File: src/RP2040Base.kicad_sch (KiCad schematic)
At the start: 14 parts, among them J1 USB4500-03-0-A, U1 RT6154AGQW

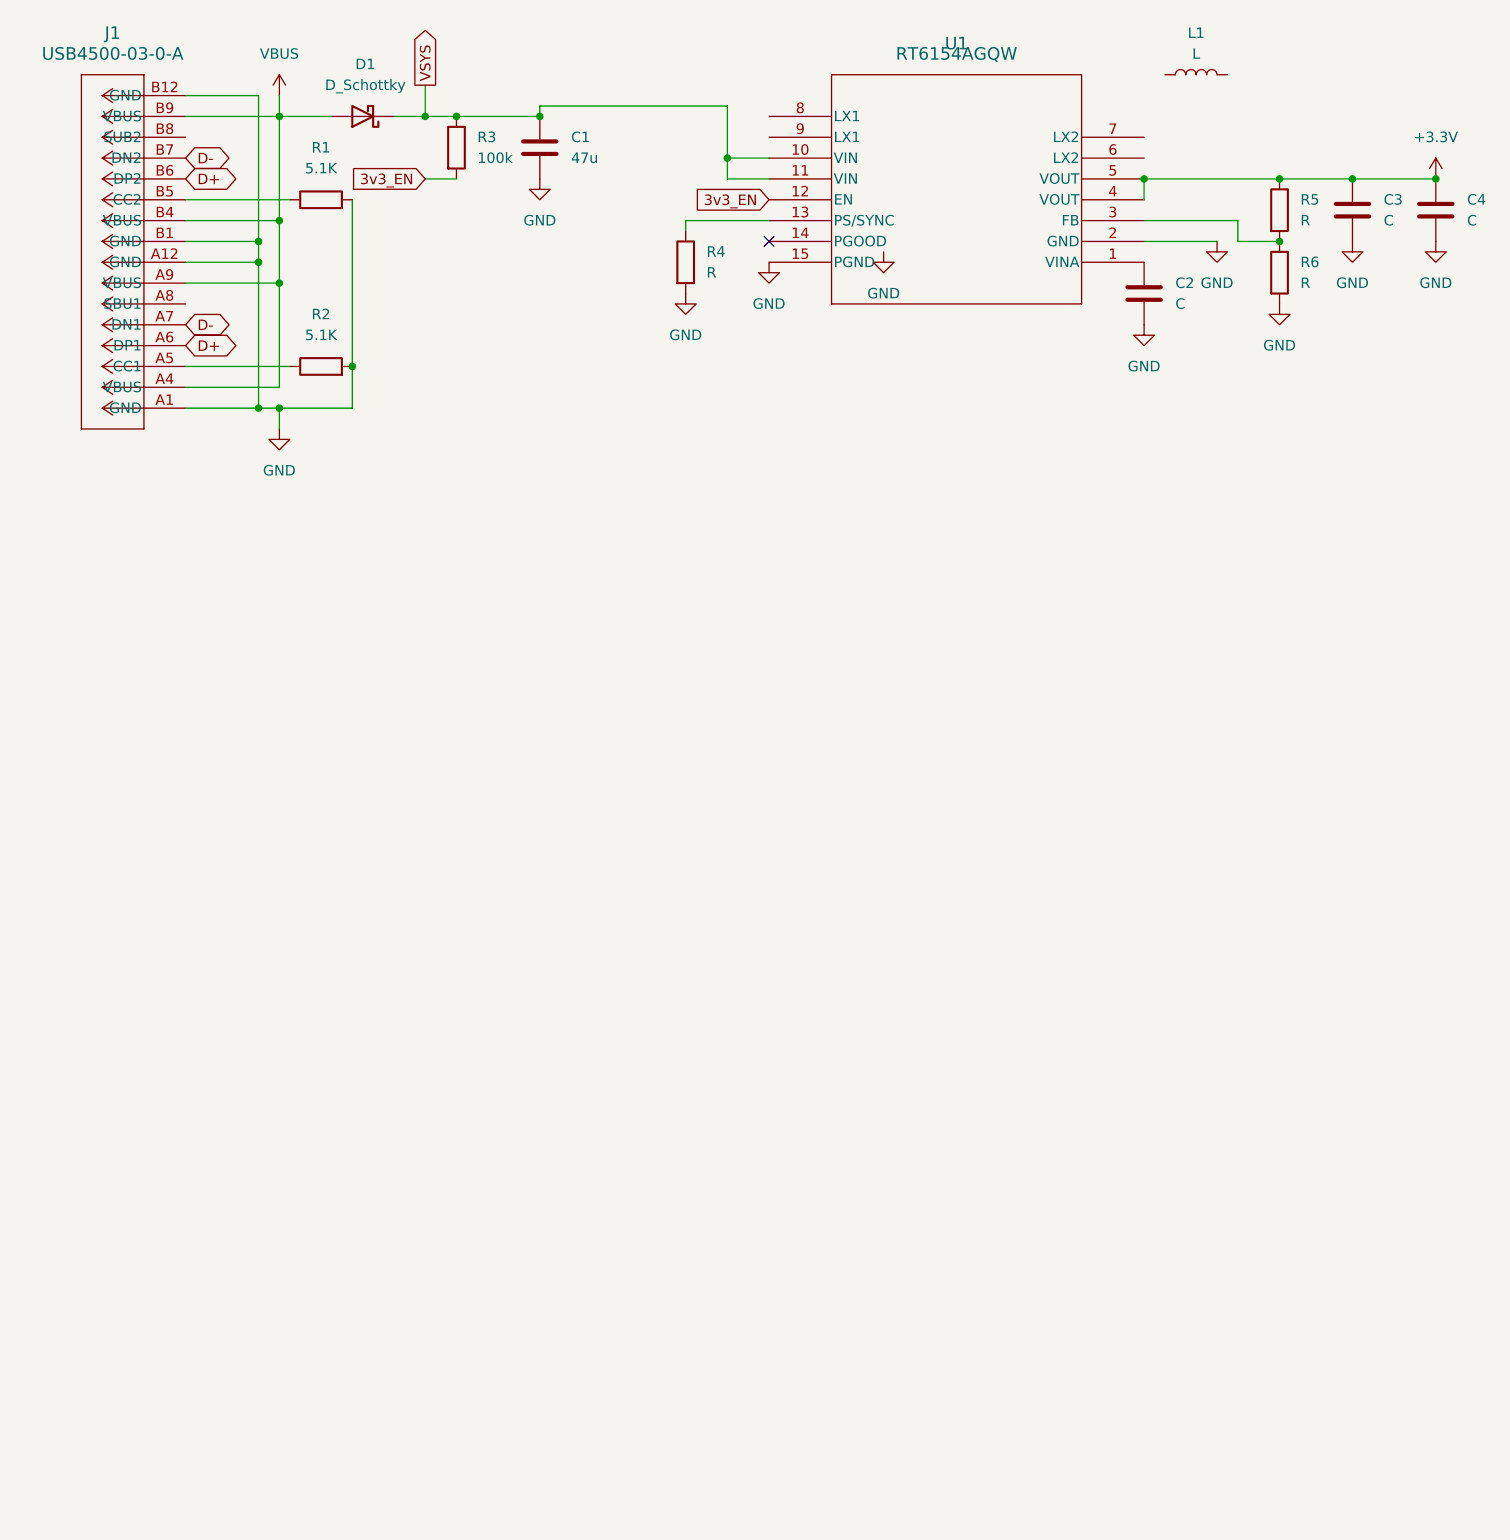
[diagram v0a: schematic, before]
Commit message: Adding Oscillator, flash, and MCU
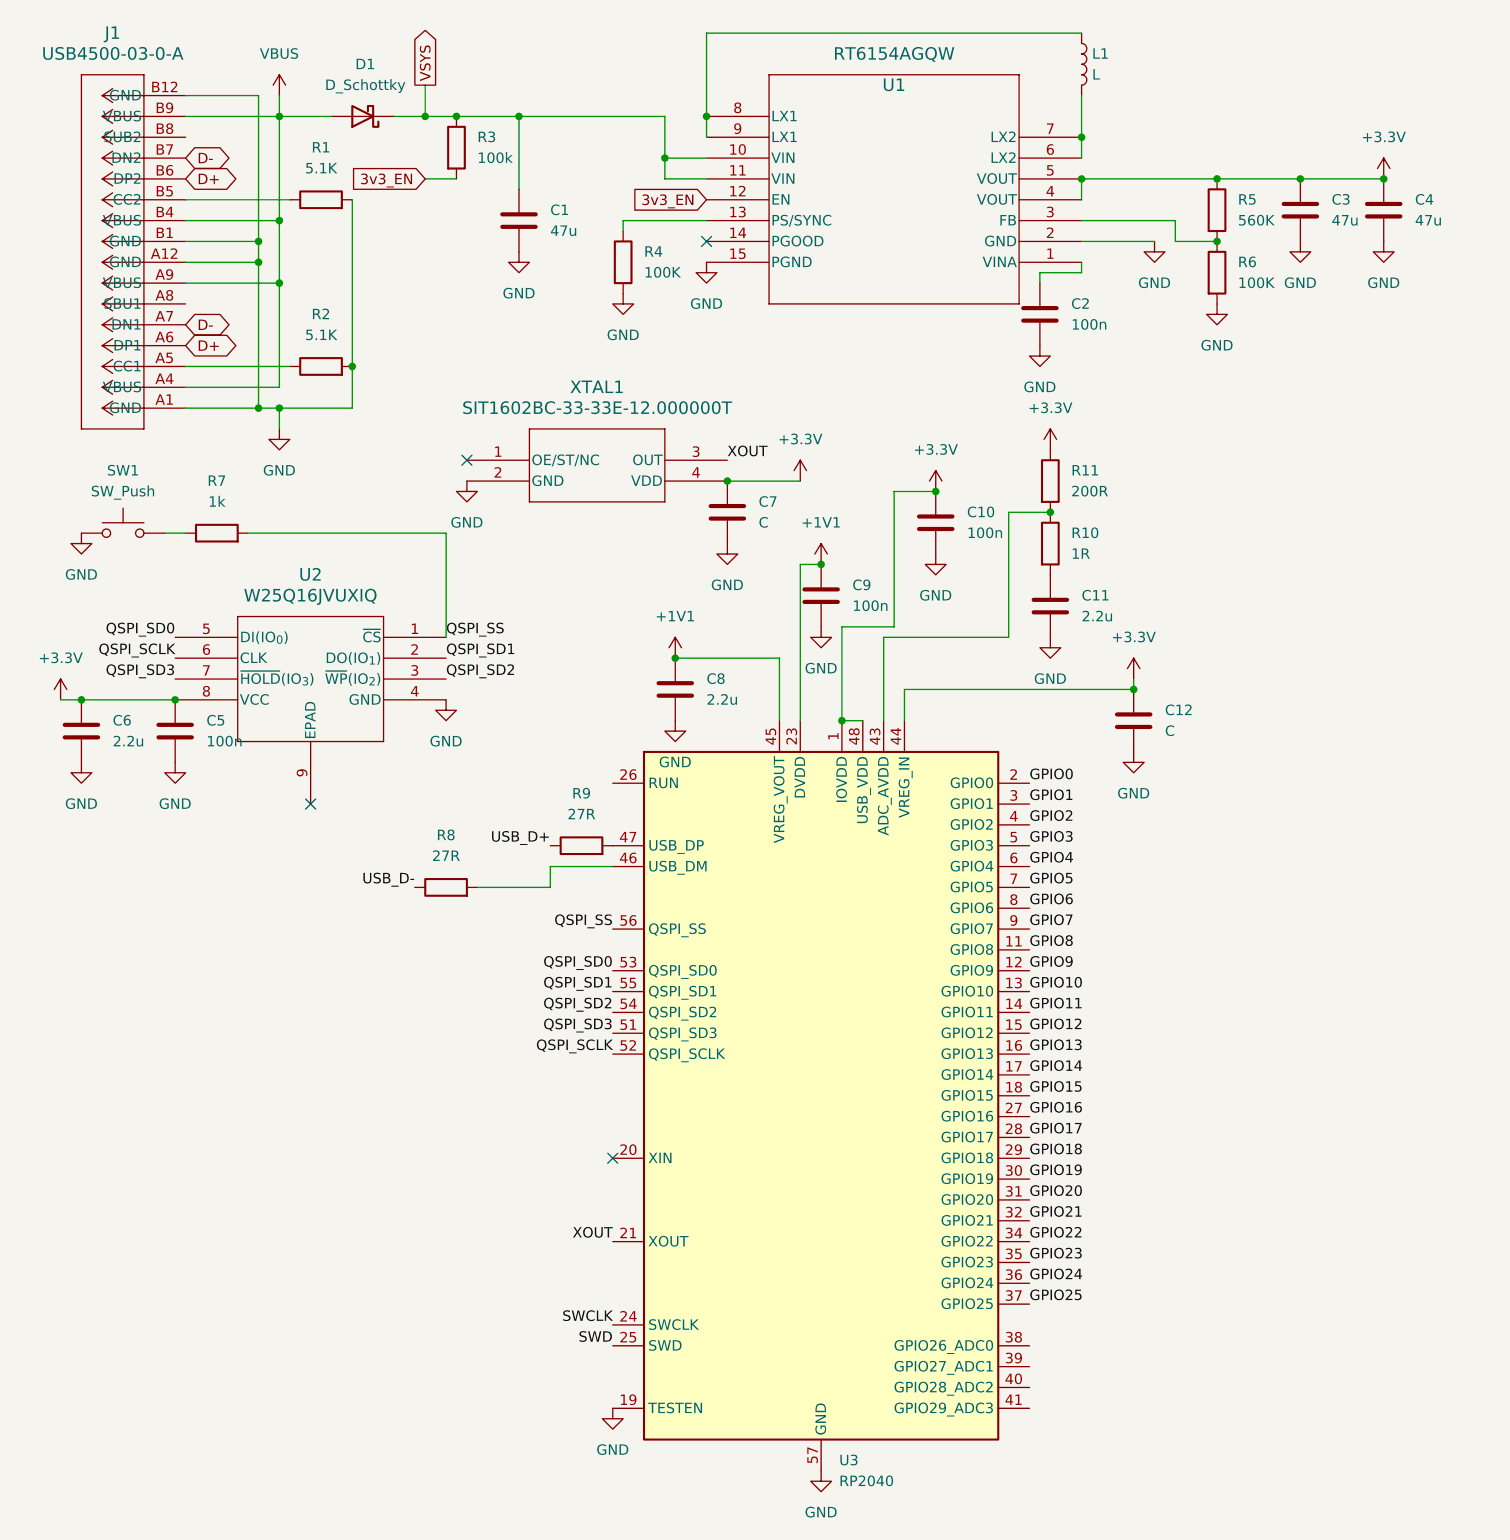
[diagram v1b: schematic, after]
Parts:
- added C10, C5, C9: 100n, symbol Device:C
- added C11, C6, C8: 2.2u, symbol Device:C
- added C12, C7: C, symbol Device:C
- added R10: 1R, symbol Device:R
- added R11: 200R, symbol Device:R
- added R7: 1k, symbol Device:R
- added R8, R9: 27R, symbol Device:R
- added SW1: SW_Push, symbol Switch:SW_Push
- added U2: W25Q16JVUXIQ, W25Q16JVUXIQ_WIN, symbol W25Q16JVUXIQ:W25Q16JVUXIQ
- added U3: RP2040, Package_DFN_QFN:QFN-56-1EP_7x7mm_P0.4mm_EP3.2x3.2mm, symbol MCU_RaspberryPi:RP2040
- added XTAL1: SIT1602BC-33-33E-12.000000T, SON4_SIT1602-3_SIT, symbol SIT1602BC:SIT1602BC-33-33E-12.000000T
- C2: value C -> 100n
- C3, C4: value C -> 47u
- R4, R6: value R -> 100K
- R5: value R -> 560K
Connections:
- net +3.3V: now also C10.1, C12.1, C5.1, C6.1, C7.1, R11.1, U2.8 (VCC), U3.1 (IOVDD), U3.10 (IOVDD), U3.22 (IOVDD), U3.33 (IOVDD), U3.42 (IOVDD), U3.44 (VREG_IN), U3.48 (USB_VDD), U3.49 (IOVDD), XTAL1.4 (VDD)
- net GND: now also C10.2, C11.2, C12.2, C5.2, C6.2, C7.2, C8.2, C9.2, SW1.1, U2.4 (GND), U3.19 (TESTEN), U3.57 (GND), XTAL1.2 (GND)
- net at U1.6 (LX2): now also L1.2, U1.7 (LX2)
- net at U1.8 (LX1): now also L1.1, U1.9 (LX1)
- new net: R10.1, R11.2, U3.43 (ADC_AVDD)
- new net: C11.1, R10.2
- new net: R9.2, U3.47 (USB_DP)
- new net: R8.2, U3.46 (USB_DM)
- new net: R7.1, SW1.2
- new net +1V1: C8.1, C9.1, U3.23 (DVDD), U3.45 (VREG_VOUT), U3.50 (DVDD)
- new net GPIO0: U3.2 (GPIO0)
- new net GPIO1: U3.3 (GPIO1)
- new net GPIO10: U3.13 (GPIO10)
- new net GPIO11: U3.14 (GPIO11)
- new net GPIO12: U3.15 (GPIO12)
- new net GPIO13: U3.16 (GPIO13)
- new net GPIO14: U3.17 (GPIO14)
- new net GPIO15: U3.18 (GPIO15)
- new net GPIO16: U3.27 (GPIO16)
- new net GPIO17: U3.28 (GPIO17)
- new net GPIO18: U3.29 (GPIO18)
- new net GPIO19: U3.30 (GPIO19)
- new net GPIO2: U3.4 (GPIO2)
- new net GPIO20: U3.31 (GPIO20)
- new net GPIO21: U3.32 (GPIO21)
- new net GPIO22: U3.34 (GPIO22)
- new net GPIO23: U3.35 (GPIO23)
- new net GPIO24: U3.36 (GPIO24)
- new net GPIO25: U3.37 (GPIO25)
- new net GPIO3: U3.5 (GPIO3)
- new net GPIO4: U3.6 (GPIO4)
- new net GPIO5: U3.7 (GPIO5)
- new net GPIO6: U3.8 (GPIO6)
- new net GPIO7: U3.9 (GPIO7)
- new net GPIO8: U3.11 (GPIO8)
- new net GPIO9: U3.12 (GPIO9)
- new net QSPI_SCLK: U2.6 (CLK), U3.52 (QSPI_SCLK)
- new net QSPI_SD0: U2.5 (DI(IO_{0})), U3.53 (QSPI_SD0)
- new net QSPI_SD1: U2.2 (DO(IO_{1})), U3.55 (QSPI_SD1)
- new net QSPI_SD2: U2.3 (~{WP}(IO_{2})), U3.54 (QSPI_SD2)
- new net QSPI_SD3: U2.7 (~{HOLD}(IO_{3})), U3.51 (QSPI_SD3)
- new net QSPI_SS: R7.2, U2.1 (~{CS}), U3.56 (QSPI_SS)
- new net SWCLK: U3.24 (SWCLK)
- new net SWD: U3.25 (SWD)
- new net USB_D+: R9.1
- new net USB_D-: R8.1
- new net XOUT: U3.21 (XOUT), XTAL1.3 (OUT)
- no-connect marks 1 -> 4
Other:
- moved on the sheet: C1, C2, C3, C4, L1, R4, R5, R6, U1
